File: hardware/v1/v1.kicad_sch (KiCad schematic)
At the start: 3 parts, among them J1 RJ45 Breakout (Winford BRK8P8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, U1 ESP32-DevKitC-32E, U2 MAX3485

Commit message: Updated title block for v1
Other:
- title: (none) -> Hot Tub Remote Controller
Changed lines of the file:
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@@
 	(generator_version "10.0")
 	(paper "A4")
+	(title_block
+		(title "Hot Tub Remote Controller")
+		(date "2026-09-05")
+		(rev "1")
+	)
 	(text_box "DE + RE~ tied to GPIO4 (UART RTS).\nLOW = receive, HIGH = transmit.\nDirection driven automatically by\nESP-IDF UART_MODE_RS485_HALF_DUPLEX\n- not bit-banged in software."
 		(exclude_from_sim no)

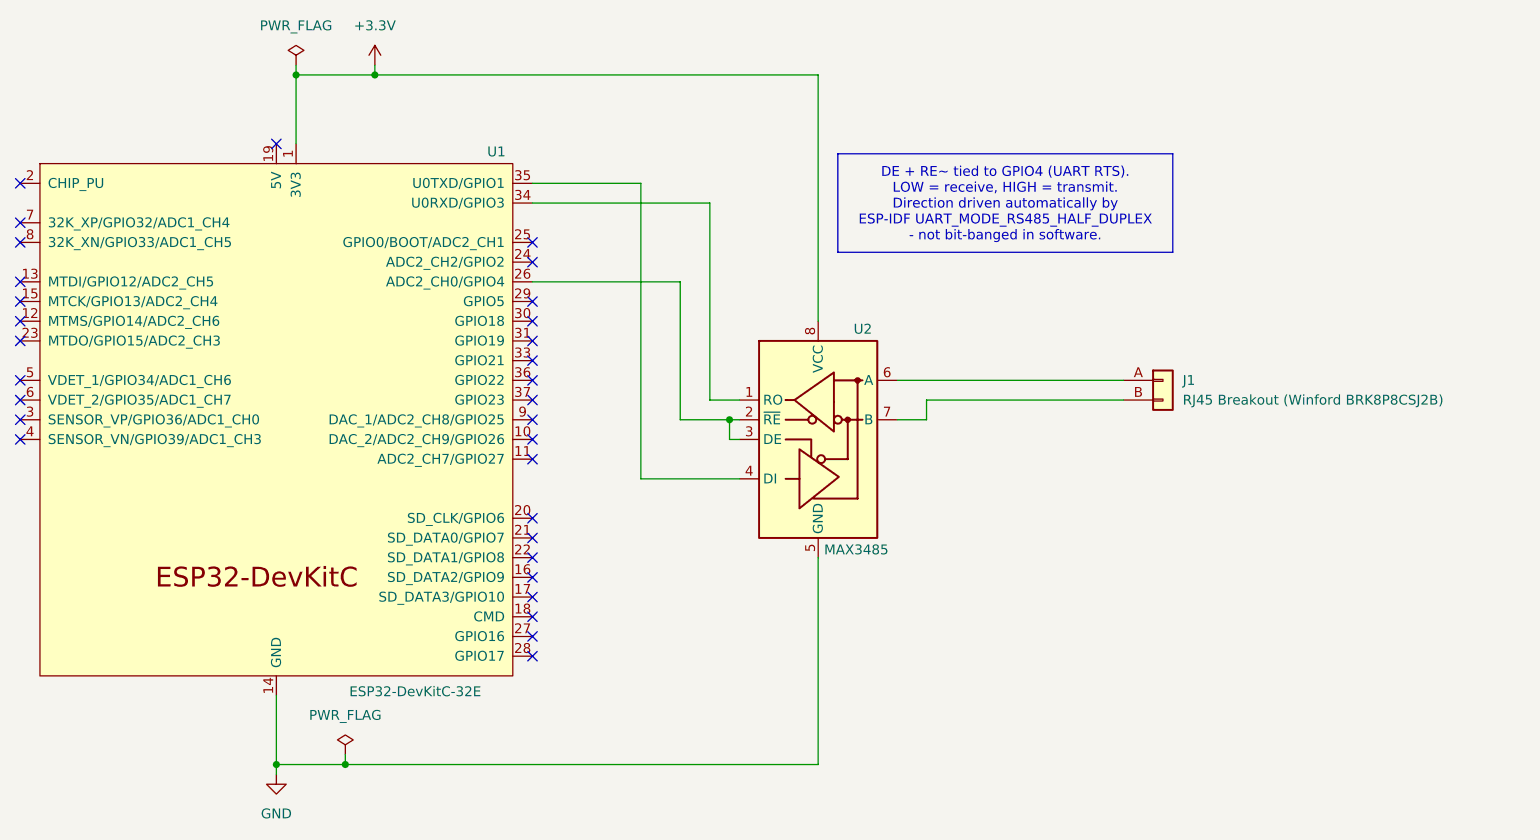
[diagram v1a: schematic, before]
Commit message: Name the RS485 nets and add a pulldown on the direction line
The schematic connected everything with bare wires and no net labels, so the
pin assignment lived only in main.c and in the jumper wires on the
breadboard. Label the five signal nets -- RS485_DI, RS485_RO, RS485_DE,
RS485_A, RS485_B -- so the GPIO choice is recorded in the hardware source
rather than inferred from firmware.

That choice was not arbitrary. GPIO17/16 are UART2's default pins and are
free on the DevKitC. GPIO1/3 are the obvious-looking candidates, being
silkscreened TX/RX, and are the wrong answer: they are hardwired to the
onboard CP2102N, so a transceiver on them contends with the USB bridge, and
worse, the ROM bootloader prints its banner out GPIO1 at every reset -- which
with DI on that pin would spray onto the spa bus while the pack and topside
panel are talking. GPIO4 for direction control is output-capable, not a
strapping pin, and clear of the SPI flash on GPIO6-11.

R1 pulls RS485_DE down. Between power-on and the moment uart_set_pin
configures GPIO4, the pin is a high-impedance input; if the transceiver's
DE/RE floats high in that window it drives the bus while the ESP32 is still
booting. The pulldown makes receive the default whenever firmware is not
actively driving the line -- the same class of hazard as the bootloader
banner, and likewise only fixable in hardware.

Nets are named for the MAX3485's own pin names, since U2 is drawn as the
chip. The breakout used on the breadboard silkscreens these as TXD (DI),
RXD (RO) and EN (DE and RE bridged internally).

Claude-Session: https://claude.ai/code/session_01KebiqHvxuNvrdmJDFb8xEN
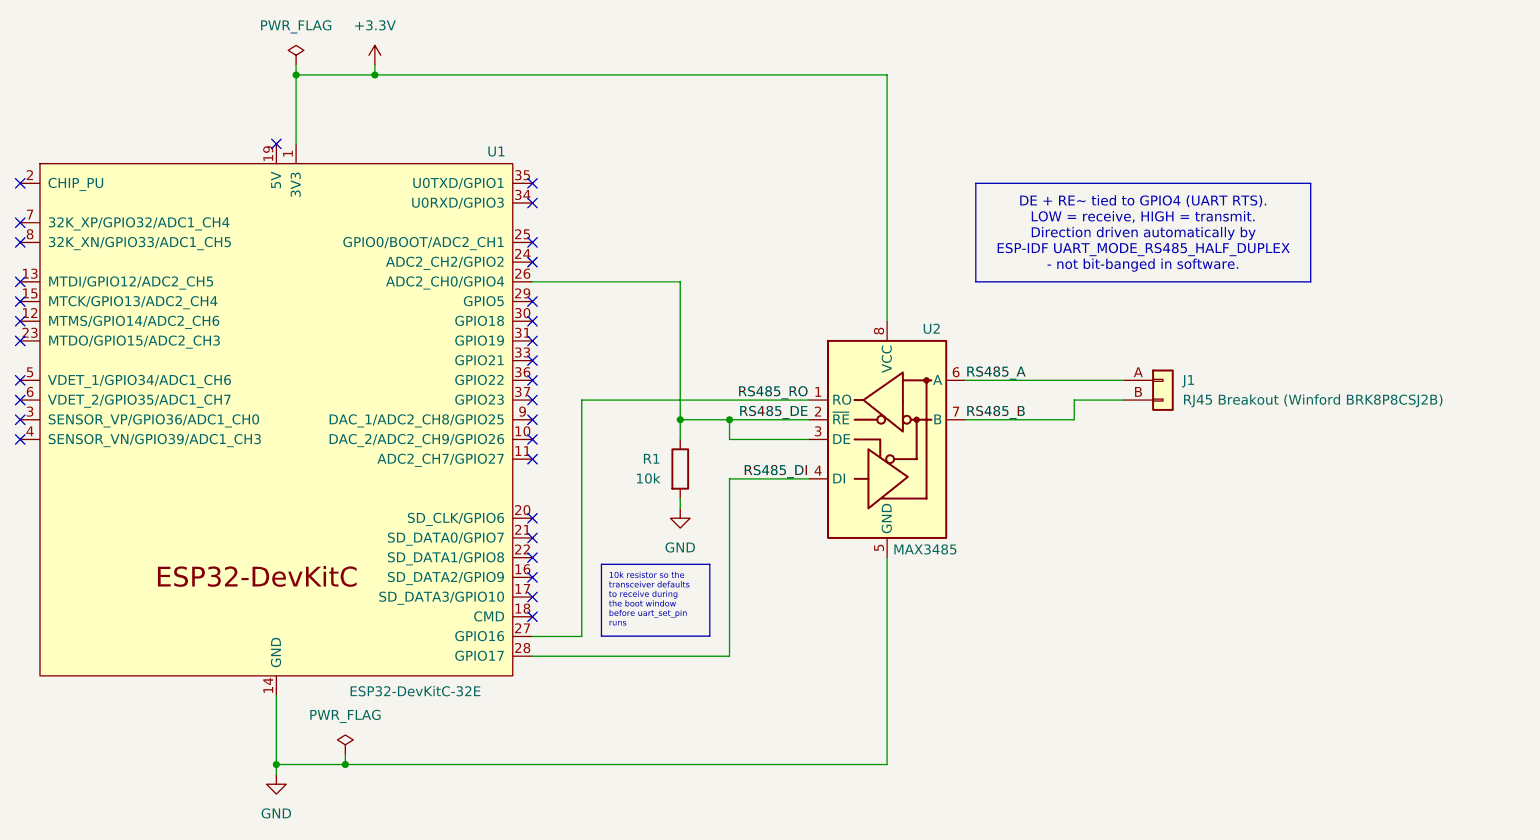
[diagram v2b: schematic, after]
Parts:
- added R1: 10k, symbol Device:R
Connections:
- net GND: now also R1.2
- net RS485_DE: now reaches U1.26 (ADC2_CH0/GPIO4), U2.2 (~{RE}), U2.3 (DE)
- net RS485_DE: now also R1.1
- net RS485_RO: now reaches U1.27 (GPIO16)
- net RS485_RO: now also U2.1 (RO)
- net RS485_DI: now reaches U1.28 (GPIO17)
- net RS485_DI: now also U2.4 (DI)
- net at U1.34 (U0RXD/GPIO3): no longer U2.1 (RO)
- net at U1.35 (U0TXD/GPIO1): no longer U2.4 (DI)
- net RS485_A: now reaches J1.A (RS485_A), U2.6 (A)
- net RS485_B: now reaches J1.B (RS485_B), U2.7 (B)
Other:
- moved on the sheet: U2
